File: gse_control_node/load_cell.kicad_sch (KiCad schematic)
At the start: 1 part, among them J3 Conn_01x05

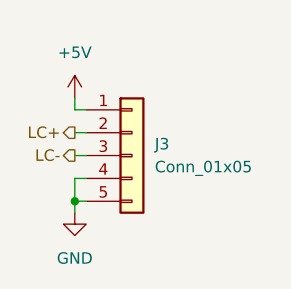
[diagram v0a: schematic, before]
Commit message: Heater/ignitor control (#2)
* update project to kicad v10

* remove thermistors from board

* rename project to be more descriptive

* fix load cell connector

* switch to on-board esp32s3

* fix fan header footprint

* update buck converter components and add reverse polarity protection

* do some pcb routing

* finish pcb routing

* remove unneccesary component fields

* add all lcsc part numbers

* add readme

* add thermal reliefs on bottom power planes

* give more clearance for load cell connector from edge of board

* fix 5.17V buck switch node net name

* switch to esp32-s3-wroom-1

* update some routing and put ground pour on top layer to avoid warping

* update silkscreen

* update all capacitors to jlcpcb basic components

* add a 12v testpoint

* update resistors to jlcpcb basic components

* fix copper pour priorities

* move up ads112c04 capacitors further from pins for easier handsoldering

* remove some extended components from bom (to be handsoldered)

* update screw terminal footprint

* add tachometer pullup and pwm low side fet for fans

* organize hierarchical sheet page numbers

* add heater connectors

* add heater power regulation for fet switching

* seperate board directories and finish heater driver routing

* add relay to heater board for estop and do some ignitor board routing

* finish ignitor board routing

* finish control board routing

* updates for manufacturing

* remove leftover files

* improve silkscreening on ignitor board and add connector for keyswitch

* make gitignore ignore production dir recursively
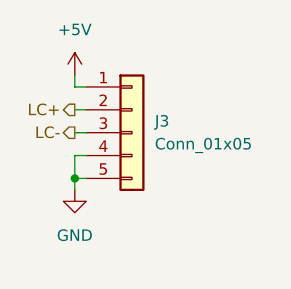
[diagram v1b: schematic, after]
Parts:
- J3: now in the parts list
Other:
- moved on the sheet: J3
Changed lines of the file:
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@@
 	(paper "A5")
 	(junction
-		(at 99.06 71.12)
+		(at 99.06 68.58)
 		(diameter 0)
 		(color 0 0 0 0)
@@
 	(wire
 		(pts
-			(xy 99.06 71.12) (xy 99.06 68.58)
-		)
-		(stroke
-			(width 0)
-			(type default)
-		)
-	)
-	(wire
-		(pts
-			(xy 99.06 59.69) (xy 99.06 60.96)
-		)
-		(stroke
-			(width 0)
-			(type default)
-		)
-	)
-	(wire
-		(pts
-			(xy 99.06 66.04) (xy 100.33 66.04)
-		)
-		(stroke
-			(width 0)
-			(type default)
-		)
-	)
-	(wire
-		(pts
-			(xy 99.06 72.39) (xy 99.06 71.12)
+			(xy 99.06 60.96) (xy 100.33 60.96)
+		)
+		(stroke
+			(width 0)
+			(type default)
+		)
+	)
+	(wire
+		(pts
+			(xy 100.33 66.04) (xy 99.06 66.04)
+		)
+		(stroke
+			(width 0)
+			(type default)
+		)
+	)
+	(wire
+		(pts
+			(xy 99.06 58.42) (xy 100.33 58.42)
+		)
+		(stroke
+			(width 0)
+			(type default)
+		)
+	)
+	(wire
+		(pts
+			(xy 99.06 57.15) (xy 99.06 58.42)
+		)
+		(stroke
+			(width 0)
+			(type default)
+		)
+	)
+	(wire
+		(pts
+			(xy 99.06 66.04) (xy 99.06 68.58)
+		)
+		(stroke
+			(width 0)
+			(type default)
+		)
+	)
+	(wire
+		(pts
+			(xy 99.06 68.58) (xy 99.06 69.85)
+		)
+		(stroke
+			(width 0)
+			(type default)
+		)
+	)
+	(wire
+		(pts
+			(xy 99.06 63.5) (xy 100.33 63.5)
 		)
 		(stroke
@@
 		)
 	)
-	(wire
-		(pts
-			(xy 99.06 60.96) (xy 100.33 60.96)
-		)
-		(stroke
-			(width 0)
-			(type default)
-		)
-	)
-	(wire
-		(pts
-			(xy 99.06 63.5) (xy 100.33 63.5)
-		)
-		(stroke
-			(width 0)
-			(type default)
-		)
-	)
-	(wire
-		(pts
-			(xy 99.06 71.12) (xy 100.33 71.12)
-		)
-		(stroke
-			(width 0)
-			(type default)
-		)
-	)
 	(hierarchical_label "LC-"
-		(shape output)
-		(at 99.06 66.04 180)
-		(effects
-			(font
-				(size 1.27 1.27)
-			)
-			(justify right)
-		)
-	)
-	(hierarchical_label "LC+"
 		(shape output)
 		(at 99.06 63.5 180)
@@
 		)
 	)
+	(hierarchical_label "LC+"
+		(shape output)
+		(at 99.06 60.96 180)
+		(effects
+			(font
+				(size 1.27 1.27)
+			)
+			(justify right)
+		)
+	)
 	(symbol
 		(lib_id "power:GND")
-		(at 99.06 72.39 0)
+		(at 99.06 69.85 0)
 		(unit 1)
 		(body_style 1)
@@
 		(fields_autoplaced yes)
 		(property "Reference" "#PWR025"
-			(at 99.06 78.74 0)
+			(at 99.06 76.2 0)
 			(hide yes)
 			(show_name no)
@@
 		)
 		(property "Value" "GND"
-			(at 99.06 77.47 0)
+			(at 99.06 74.93 0)
 			(show_name no)
 			(do_not_autoplace no)
@@
 		)
 		(property "Footprint" ""
-			(at 99.06 72.39 0)
+			(at 99.06 69.85 0)
 			(hide yes)
 			(show_name no)
@@
 		)
 		(property "Datasheet" ""
-			(at 99.06 72.39 0)
+			(at 99.06 69.85 0)
 			(hide yes)
 			(show_name no)
@@
 		)
 		(property "Description" "Power symbol creates a global label with name \"GND\" , ground"
-			(at 99.06 72.39 0)
+			(at 99.06 69.85 0)
 			(hide yes)
 			(show_name no)
@@
 	(symbol
 		(lib_id "power:+5V")
-		(at 99.06 59.69 0)
+		(at 99.06 57.15 0)
 		(unit 1)
 		(body_style 1)
@@
 		(fields_autoplaced yes)
 		(property "Reference" "#PWR024"
-			(at 99.06 63.5 0)
+			(at 99.06 60.96 0)
 			(hide yes)
 			(show_name no)
@@
 		)
 		(property "Value" "+5V"
-			(at 99.06 54.61 0)
+			(at 99.06 52.07 0)
 			(show_name no)
 			(do_not_autoplace no)
@@
 		)
 		(property "Footprint" ""
-			(at 99.06 59.69 0)
+			(at 99.06 57.15 0)
 			(hide yes)
 			(show_name no)
@@
 		)
 		(property "Datasheet" ""
-			(at 99.06 59.69 0)
+			(at 99.06 57.15 0)
 			(hide yes)
 			(show_name no)
@@
 		)
 		(property "Description" "Power symbol creates a global label with name \"+5V\""
-			(at 99.06 59.69 0)
+			(at 99.06 57.15 0)
 			(hide yes)
 			(show_name no)
@@
 	(symbol
 		(lib_id "Connector_Generic:Conn_01x05")
-		(at 105.41 66.04 0)
+		(at 105.41 63.5 0)
 		(unit 1)
 		(body_style 1)
 		(exclude_from_sim no)
-		(in_bom no)
+		(in_bom yes)
 		(on_board yes)
-		(in_pos_files no)
+		(in_pos_files yes)
 		(dnp no)
 		(fields_autoplaced yes)
 		(property "Reference" "J3"
+			(at 107.95 62.2299 0)
+			(show_name no)
+			(do_not_autoplace no)
+			(effects
+				(font
+					(size 1.27 1.27)
+				)
+				(justify left)
+			)
+		)
+		(property "Value" "Conn_01x05"
 			(at 107.95 64.7699 0)
 			(show_name no)
@@
 			)
 		)
-		(property "Value" "Conn_01x05"
-			(at 107.95 67.3099 0)
-			(show_name no)
-			(do_not_autoplace no)
-			(effects
-				(font
-					(size 1.27 1.27)
-				)
-				(justify left)
-			)
-		)
 		(property "Footprint" "Connector_Molex:Molex_Micro-Fit_3.0_43650-0515_1x05_P3.00mm_Vertical"
-			(at 105.41 66.04 0)
+			(at 105.41 63.5 0)
 			(hide yes)
 			(show_name no)
@@
 		)
 		(property "Datasheet" ""
-			(at 105.41 66.04 0)
+			(at 105.41 63.5 0)
 			(hide yes)
 			(show_name no)
@@
 		)
 		(property "Description" "Generic connector, single row, 01x05, script generated (kicad-library-utils/schlib/autogen/connector/)"
-			(at 105.41 66.04 0)
+			(at 105.41 63.5 0)
 			(hide yes)
 			(show_name no)
@@
 		)
 		(property "LCSC" "N/A"
-			(at 105.41 66.04 0)
-			(hide yes)
-			(show_name no)
+			(at 105.41 63.5 0)
+			(hide yes)
+			(show_name no)
